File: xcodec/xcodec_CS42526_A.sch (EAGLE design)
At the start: 73 parts, among them J2 PINHD-3X9/90, J3 PINHD-3X7/90, U1 CS42526, U2 FIN1002, U3 FIN1002

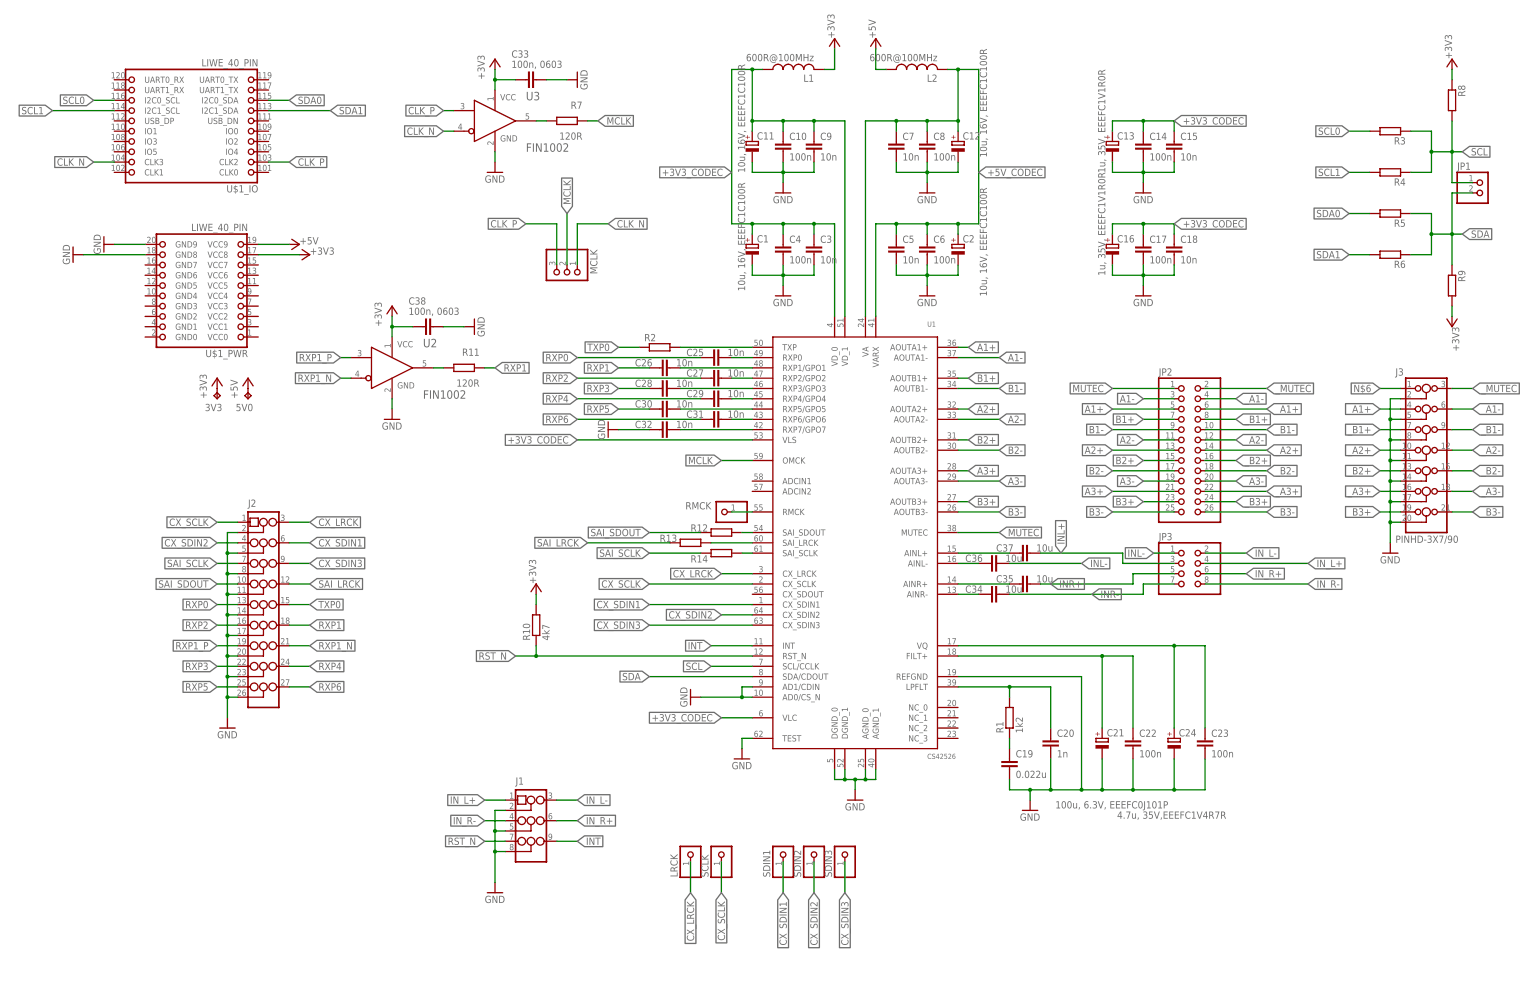
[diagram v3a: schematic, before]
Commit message: xcodec: finished PCB.
Signed-off-by: malo <pavol.malosek@gmail.com>
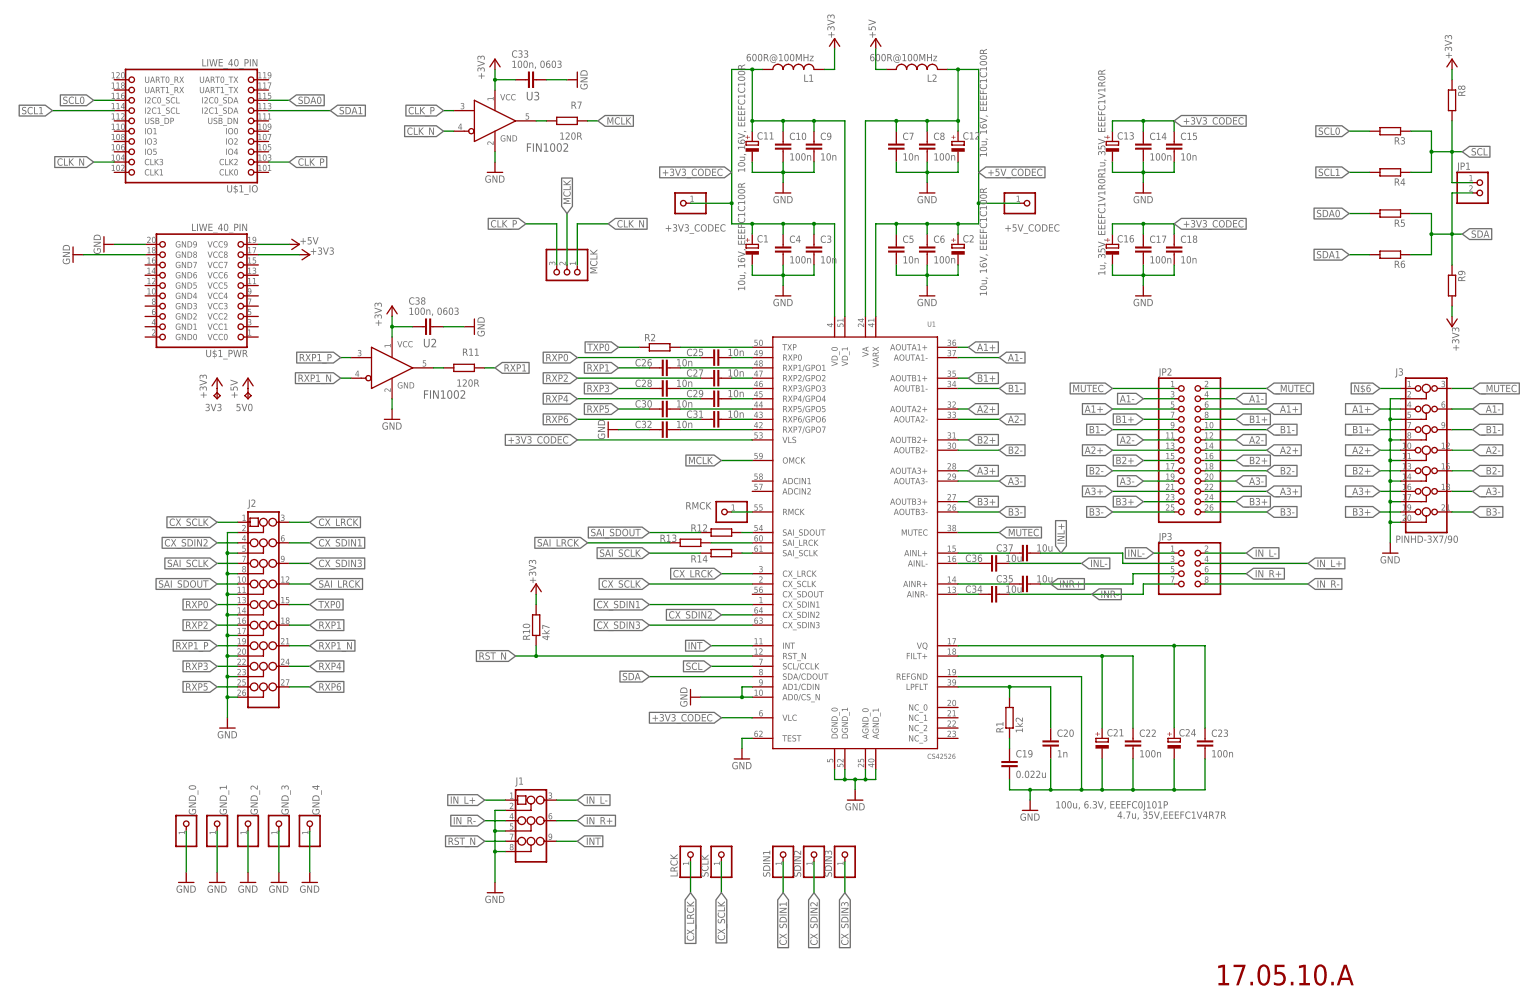
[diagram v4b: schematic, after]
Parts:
- added +3V3_CODEC, +5V_CODEC, GND_0, GND_1, GND_2, GND_3, GND_4: (no value), 25pinhead:PINHD-1X1
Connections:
- net +3V3_CODEC: now also +3V3_CODEC.1
- net +5V_CODEC: now also +5V_CODEC.1
- net GND: now also GND_0.1, GND_1.1, GND_2.1, GND_3.1, GND_4.1
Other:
- note added: "17.05.10.A"
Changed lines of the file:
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@@
 <?xml version="1.0" encoding="utf-8"?>
 <!DOCTYPE eagle SYSTEM "eagle.dtd">
-<eagle version="8.1.0">
+<eagle version="8.2.0">
 <drawing>
 <settings>
@@
 <part name="GND17" library="supply1" deviceset="GND" device=""/>
 <part name="GND18" library="supply1" deviceset="GND" device=""/>
+<part name="+3V3_CODEC" library="25pinhead" deviceset="PINHD-1X1" device=""/>
+<part name="+5V_CODEC" library="25pinhead" deviceset="PINHD-1X1" device=""/>
+<part name="GND_0" library="25pinhead" deviceset="PINHD-1X1" device=""/>
+<part name="GND_1" library="25pinhead" deviceset="PINHD-1X1" device=""/>
+<part name="GND_2" library="25pinhead" deviceset="PINHD-1X1" device=""/>
+<part name="GND_3" library="25pinhead" deviceset="PINHD-1X1" device=""/>
+<part name="GND_4" library="25pinhead" deviceset="PINHD-1X1" device=""/>
+<part name="GND19" library="supply1" deviceset="GND" device=""/>
+<part name="GND20" library="supply1" deviceset="GND" device=""/>
+<part name="GND21" library="supply1" deviceset="GND" device=""/>
+<part name="GND22" library="supply1" deviceset="GND" device=""/>
+<part name="GND23" library="supply1" deviceset="GND" device=""/>
 </parts>
 <sheets>
 <sheet>
 <plain>
+<text x="299.72" y="12.7" size="5.08" layer="94">17.05.10.A</text>
 </plain>
 <instances>
@@
 <instance part="GND17" gate="1" x="25.4" y="195.58" rot="R270"/>
 <instance part="GND18" gate="1" x="17.78" y="193.04" rot="R270"/>
+<instance part="+3V3_CODEC" gate="G$1" x="167.64" y="205.74" smashed="yes" rot="R180">
+<attribute name="NAME" x="163.83" y="198.755" size="1.778" layer="95"/>
+<attribute name="VALUE" x="173.99" y="210.82" size="1.778" layer="96" rot="R180"/>
+</instance>
+<instance part="+5V_CODEC" gate="G$1" x="254" y="205.74" smashed="yes">
+<attribute name="NAME" x="247.65" y="198.755" size="1.778" layer="95"/>
+<attribute name="VALUE" x="247.65" y="200.66" size="1.778" layer="96"/>
+</instance>
+<instance part="GND_0" gate="G$1" x="45.72" y="53.34" smashed="yes" rot="R90">
+<attribute name="NAME" x="46.355" y="62.23" size="1.778" layer="95" rot="R270"/>
+<attribute name="VALUE" x="50.8" y="46.99" size="1.778" layer="96" rot="R90"/>
+</instance>
+<instance part="GND_1" gate="G$1" x="53.34" y="53.34" smashed="yes" rot="R90">
+<attribute name="NAME" x="53.975" y="62.23" size="1.778" layer="95" rot="R270"/>
+<attribute name="VALUE" x="58.42" y="46.99" size="1.778" layer="96" rot="R90"/>
+</instance>
+<instance part="GND_2" gate="G$1" x="60.96" y="53.34" smashed="yes" rot="R90">
+<attribute name="NAME" x="61.595" y="62.23" size="1.778" layer="95" rot="R270"/>
+<attribute name="VALUE" x="66.04" y="46.99" size="1.778" layer="96" rot="R90"/>
+</instance>
+<instance part="GND_3" gate="G$1" x="68.58" y="53.34" smashed="yes" rot="R90">
+<attribute name="NAME" x="69.215" y="62.23" size="1.778" layer="95" rot="R270"/>
+<attribute name="VALUE" x="73.66" y="46.99" size="1.778" layer="96" rot="R90"/>
+</instance>
+<instance part="GND_4" gate="G$1" x="76.2" y="53.34" smashed="yes" rot="R90">
+<attribute name="NAME" x="76.835" y="62.23" size="1.778" layer="95" rot="R270"/>
+<attribute name="VALUE" x="81.28" y="46.99" size="1.778" layer="96" rot="R90"/>
+</instance>
+<instance part="GND19" gate="1" x="45.72" y="38.1"/>
+<instance part="GND20" gate="1" x="53.34" y="38.1"/>
+<instance part="GND21" gate="1" x="60.96" y="38.1"/>
+<instance part="GND22" gate="1" x="68.58" y="38.1"/>
+<instance part="GND23" gate="1" x="76.2" y="38.1"/>
 </instances>
 <busses>
@@
 <wire x1="35.56" y1="193.04" x2="20.32" y2="193.04" width="0.1524" layer="91"/>
 </segment>
+<segment>
+<pinref part="GND_0" gate="G$1" pin="1"/>
+<wire x1="45.72" y1="50.8" x2="45.72" y2="40.64" width="0.1524" layer="91"/>
+<pinref part="GND19" gate="1" pin="GND"/>
+</segment>
+<segment>
+<pinref part="GND_1" gate="G$1" pin="1"/>
+<wire x1="53.34" y1="50.8" x2="53.34" y2="40.64" width="0.1524" layer="91"/>
+<pinref part="GND20" gate="1" pin="GND"/>
+</segment>
+<segment>
+<pinref part="GND_2" gate="G$1" pin="1"/>
+<wire x1="60.96" y1="50.8" x2="60.96" y2="40.64" width="0.1524" layer="91"/>
+<pinref part="GND21" gate="1" pin="GND"/>
+</segment>
+<segment>
+<pinref part="GND_3" gate="G$1" pin="1"/>
+<wire x1="68.58" y1="50.8" x2="68.58" y2="40.64" width="0.1524" layer="91"/>
+<pinref part="GND22" gate="1" pin="GND"/>
+</segment>
+<segment>
+<pinref part="GND_4" gate="G$1" pin="1"/>
+<wire x1="76.2" y1="50.8" x2="76.2" y2="40.64" width="0.1524" layer="91"/>
+<pinref part="GND23" gate="1" pin="GND"/>
+</segment>
 </net>
 <net name="+3V3" class="0">
@@
 <wire x1="185.42" y1="200.66" x2="180.34" y2="200.66" width="0.1524" layer="91"/>
 <junction x="185.42" y="200.66"/>
-<wire x1="180.34" y1="200.66" x2="180.34" y2="238.76" width="0.1524" layer="91"/>
+<wire x1="180.34" y1="200.66" x2="180.34" y2="205.74" width="0.1524" layer="91"/>
 <pinref part="C9" gate="G$1" pin="1"/>
+<wire x1="180.34" y1="205.74" x2="180.34" y2="238.76" width="0.1524" layer="91"/>
 <wire x1="200.66" y1="223.52" x2="200.66" y2="226.06" width="0.1524" layer="91"/>
 <wire x1="200.66" y1="226.06" x2="193.04" y2="226.06" width="0.1524" layer="91"/>
@@
 <junction x="185.42" y="238.76"/>
 <label x="180.34" y="213.36" size="1.778" layer="95" rot="R180" xref="yes"/>
+<pinref part="+3V3_CODEC" gate="G$1" pin="1"/>
+<wire x1="170.18" y1="205.74" x2="180.34" y2="205.74" width="0.1524" layer="91"/>
+<junction x="180.34" y="205.74"/>
 </segment>
 <segment>
@@
 <wire x1="236.22" y1="200.66" x2="241.3" y2="200.66" width="0.1524" layer="91"/>
 <junction x="236.22" y="200.66"/>
-<wire x1="241.3" y1="200.66" x2="241.3" y2="238.76" width="0.1524" layer="91"/>
+<wire x1="241.3" y1="200.66" x2="241.3" y2="205.74" width="0.1524" layer="91"/>
 <pinref part="U1" gate="G$1" pin="VA"/>
+<wire x1="241.3" y1="205.74" x2="241.3" y2="238.76" width="0.1524" layer="91"/>
 <wire x1="213.36" y1="177.8" x2="213.36" y2="226.06" width="0.1524" layer="91"/>
 <pinref part="C12" gate="G$1" pin="+"/>
@@
 <junction x="236.22" y="238.76"/>
 <label x="241.3" y="213.36" size="1.778" layer="95" xref="yes"/>
+<pinref part="+5V_CODEC" gate="G$1" pin="1"/>
+<wire x1="251.46" y1="205.74" x2="241.3" y2="205.74" width="0.1524" layer="91"/>
+<junction x="241.3" y="205.74"/>
 </segment>
 </net>
